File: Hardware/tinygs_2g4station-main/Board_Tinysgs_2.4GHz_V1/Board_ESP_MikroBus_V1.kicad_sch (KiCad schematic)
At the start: 18 parts

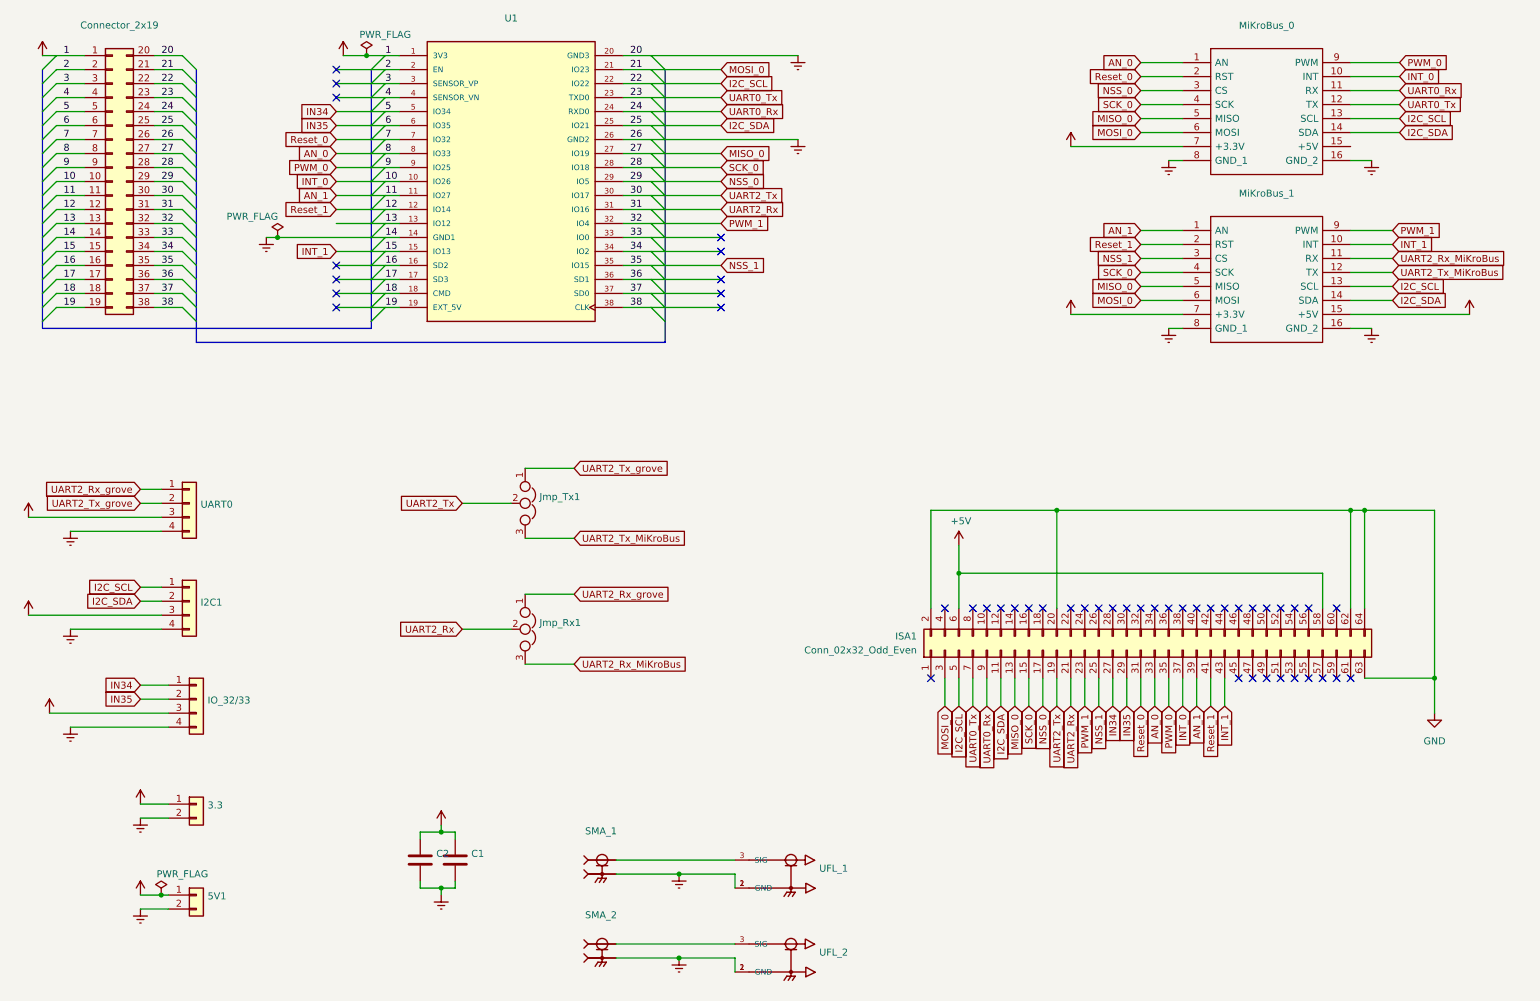
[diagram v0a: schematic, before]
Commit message: The TinyGS in cubesat standard with ISA communication is done, all the wires are branched. Verification needed to ensure it's functionality and noise/EM immunity
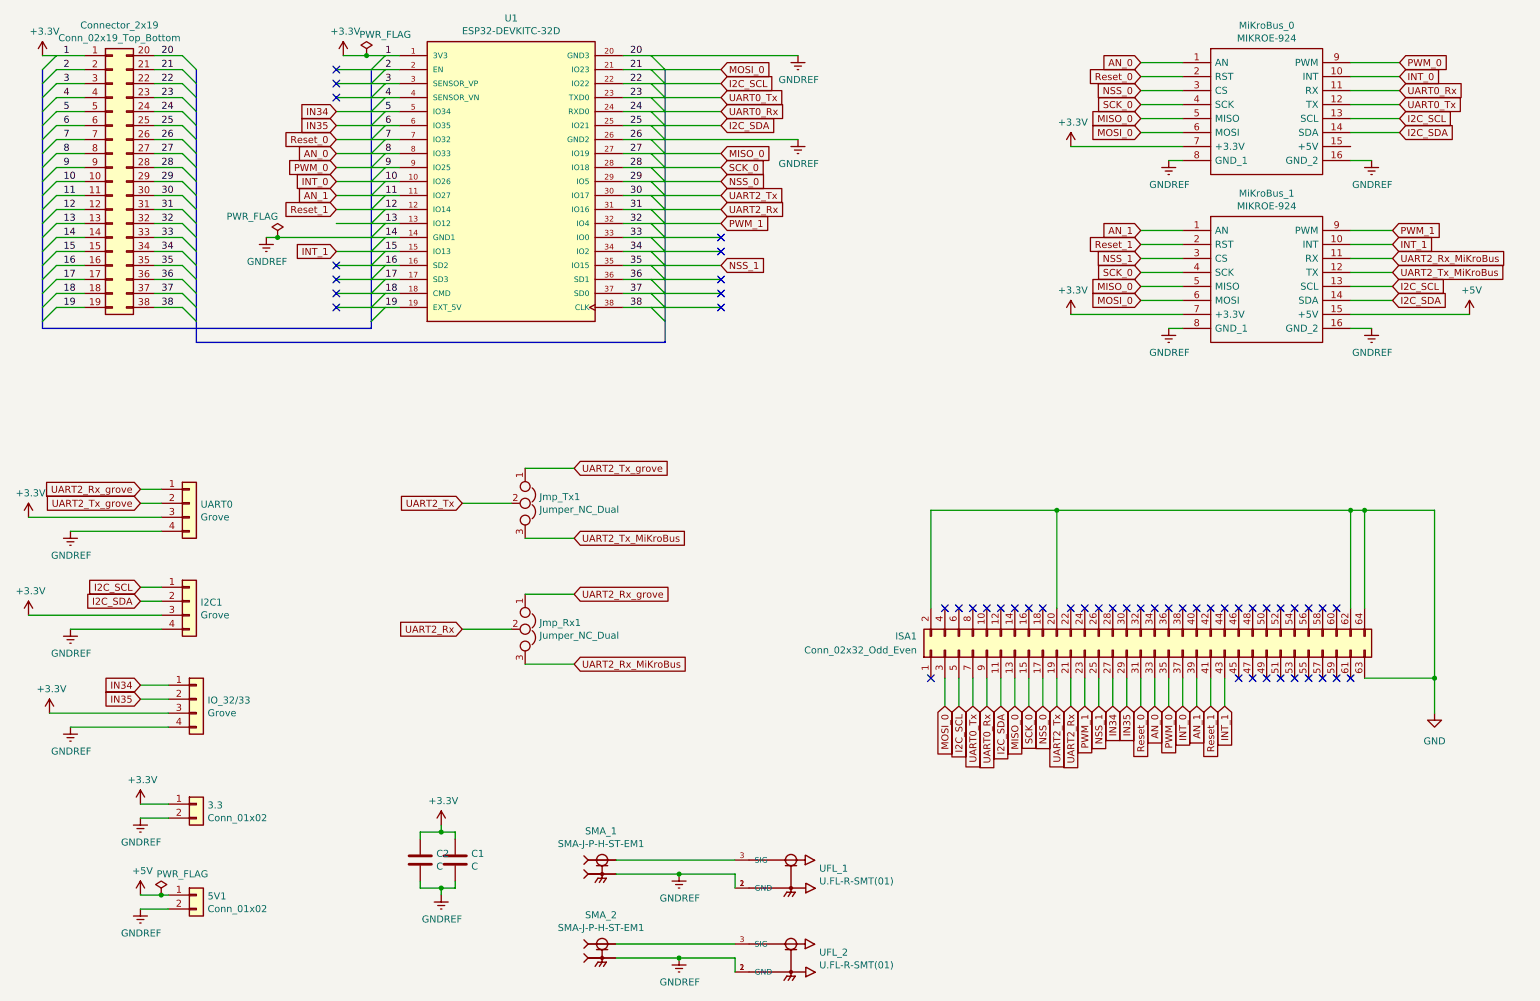
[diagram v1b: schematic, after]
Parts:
- 3.3, 5V1: value (none) -> Conn_01x02; footprint (none) -> Connector_PinHeader_2.54mm:PinHeader_1x02_P2.54mm_Vertical
- C1: value (none) -> C; footprint (none) -> Connector_PinHeader_2.54mm:PinHeader_1x02_P2.54mm_Vertical
- C2: value (none) -> C; footprint (none) -> Capacitor_SMD:C_0805_2012Metric_Pad1.18x1.45mm_HandSolder
- Connector_2x19: value (none) -> Conn_02x19_Top_Bottom; footprint (none) -> test connecteur:conn_2x19_2.54mm_top_bot
- I2C1, IO_32/33, UART0: value (none) -> Grove; footprint (none) -> Grove:Grove_4pin-2.00mm
- Jmp_Rx1, Jmp_Tx1: value (none) -> Jumper_NC_Dual; footprint (none) -> Connector_PinHeader_2.54mm:PinHeader_1x03_P2.54mm_Vertical
- MiKroBus_0, MiKroBus_1: value (none) -> MIKROE-924; footprint (none) -> MIKROE-924:MIKROE924
- SMA_1, SMA_2: value (none) -> SMA-J-P-H-ST-EM1; footprint (none) -> SMA-J-P-H-ST-EM1:SAMTEC_SMA-J-P-H-ST-EM1
- U1: value (none) -> ESP32-DEVKITC-32D; footprint (none) -> ESP32-DEVKITC-32D:MODULE_ESP32-DEVKITC-32D
- UFL_1, UFL_2: value (none) -> U.FL-R-SMT(01); footprint (none) -> U:HRS_U.FL-R-SMT(01)
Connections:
- net +5V: no longer ISA1.58 (Pin_58), ISA1.6 (Pin_6)
- no-connect marks 48 -> 50
